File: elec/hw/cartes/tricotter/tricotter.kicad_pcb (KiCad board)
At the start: 2 copper layers, 64 parts, among them J1 XT60PW-M, J2 3-794618-4, J3 3-794618-4, J4 3-794618-4, J5 3-794618-4, J6 3-794618-4, J7 22272041, Q1 2N7002, Q10 G120P06M, Q2 G120P06M, Q3 2N7002, Q4 G120P06M, Q5 2N7002, Q6 2N7002, Q7 G120P06M, Q8 G120P06M, Q9 2N7002

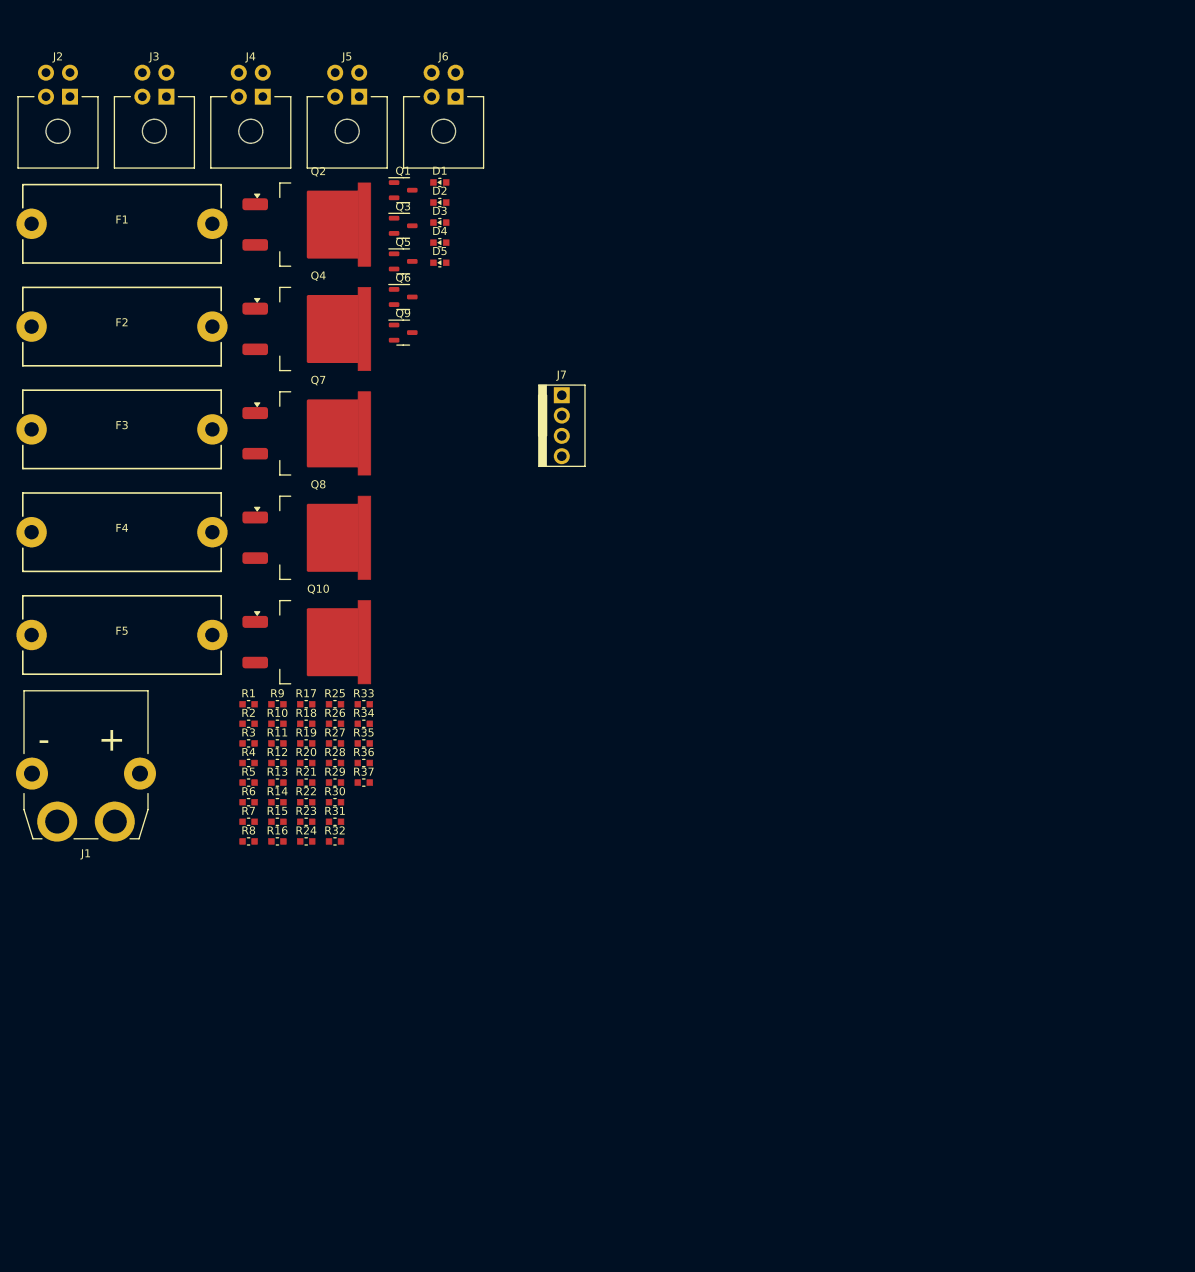
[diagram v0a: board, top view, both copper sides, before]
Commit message: tricotter board routed
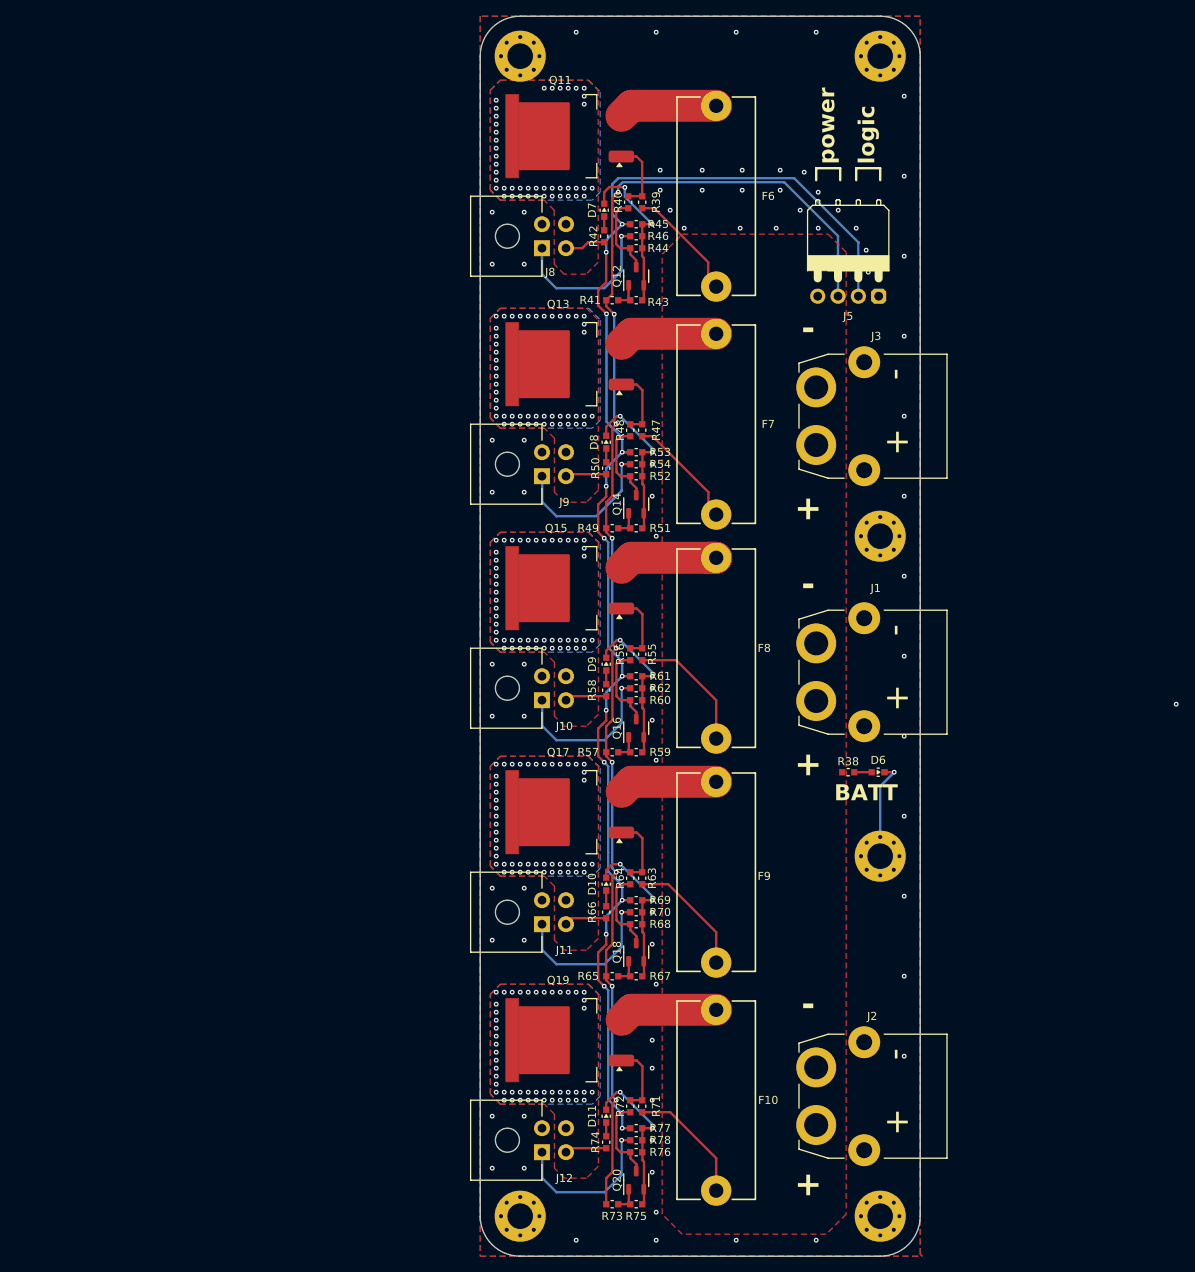
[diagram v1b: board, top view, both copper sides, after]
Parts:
- removed D1, D2, D3, D4, D5: green, 0603, cocotter_diodes:LED_0603_1608Metric
- removed F1, F2, F3, F4, F5: FH1-200CK-B, cocotter_others:FUSEHOLDER_5x20mm
- removed J4, J6: 3-794618-4, cocotter_connectors:3-794618-4
- removed J7: 22272041, cocotter_connectors:22272041
- removed Q1, Q3, Q5, Q6, Q9: 2N7002, cocotter_transistors:SOT-23-3
- removed Q10, Q2, Q4, Q7, Q8: G120P06M, cocotter_transistors:TO-263-2-GOFORD
- removed R1, R11, R12, R16, R17, R18, R19, R2, R20, R21, R25, R26, R3, R31, R32, R33, R34, R4, R5, R6: 100k, cocotter_resistor:r0603_reflow
- removed R10, R13, R14, R22, R23, R24, R28, R29, R35, R36, R7, R8: 0R, cocotter_resistor:r0603_reflow
- removed R15, R27, R30, R37, R9: 10k 1%, cocotter_resistor:r0603_reflow
- added D10: green, 0603, cocotter_diodes:LED_0603_1608Metric, F.Cu at (115.8, 133.5)
- added D11: green, 0603, cocotter_diodes:LED_0603_1608Metric, F.Cu at (115.8, 162.5)
- added D6: white, 0603, cocotter_diodes:LED_0603_1608Metric, F.Cu at (149.8, 119.5)
- added D7: green, 0603, cocotter_diodes:LED_0603_1608Metric, F.Cu at (115.5, 49.2)
- added D8: green, 0603, cocotter_diodes:LED_0603_1608Metric, F.Cu at (115.8, 78.2)
- added D9: green, 0603, cocotter_diodes:LED_0603_1608Metric, F.Cu at (115.8, 106.0)
- added F10: FH1-200CK-B, cocotter_others:FUSEHOLDER_5x20mm, F.Cu at (129.5, 160.5)
- added F6: FH1-200CK-B, cocotter_others:FUSEHOLDER_5x20mm, F.Cu at (129.5, 47.5)
- added F7: FH1-200CK-B, cocotter_others:FUSEHOLDER_5x20mm, F.Cu at (129.5, 76.0)
- added F8: FH1-200CK-B, cocotter_others:FUSEHOLDER_5x20mm, F.Cu at (129.5, 104.0)
- added F9: FH1-200CK-B, cocotter_others:FUSEHOLDER_5x20mm, F.Cu at (129.5, 132.0)
- added H1: MountingHole_Pad_M3, cocotter_others:MountingHole_3.2mm_M3_Pad_Via, F.Cu at (105.0, 175.0)
- added H2: MountingHole_Pad_M3, cocotter_others:MountingHole_3.2mm_M3_Pad_Via, F.Cu at (150.0, 175.0)
- added H3: MountingHole_Pad_M3, cocotter_others:MountingHole_3.2mm_M3_Pad_Via, F.Cu at (150.0, 30.0)
- added H4: MountingHole_Pad_M3, cocotter_others:MountingHole_3.2mm_M3_Pad_Via, F.Cu at (105.0, 30.0)
- added H5: MountingHole_Pad_M3, cocotter_others:MountingHole_3.2mm_M3_Pad_Via, F.Cu at (150.0, 90.0)
- added H6: MountingHole_Pad_M3, cocotter_others:MountingHole_3.2mm_M3_Pad_Via, F.Cu at (150.0, 130.0)
- added J10: 3-794618-4, cocotter_connectors:3-794618-4, F.Cu at (109.2, 109.0)
- added J11: 3-794618-4, cocotter_connectors:3-794618-4, F.Cu at (109.2, 137.0)
- added J12: 3-794618-4, cocotter_connectors:3-794618-4, F.Cu at (109.2, 165.5)
- added J8: 3-794618-4, cocotter_connectors:3-794618-4, F.Cu at (109.2, 52.5)
- added J9: 3-794618-4, cocotter_connectors:3-794618-4, F.Cu at (109.2, 81.0)
- added Q11: G120P06M, cocotter_transistors:TO-263-2-GOFORD, F.Cu at (109.8, 40.0)
- added Q12: 2N7002, cocotter_transistors:SOT-23-3, F.Cu at (119.5, 57.5)
- added Q13: G120P06M, cocotter_transistors:TO-263-2-GOFORD, F.Cu at (109.8, 68.5)
- added Q14: 2N7002, cocotter_transistors:SOT-23-3, F.Cu at (119.5, 86.0)
- added Q15: G120P06M, cocotter_transistors:TO-263-2-GOFORD, F.Cu at (109.8, 96.5)
- added Q16: 2N7002, cocotter_transistors:SOT-23-3, F.Cu at (119.5, 114.0)
- added Q17: G120P06M, cocotter_transistors:TO-263-2-GOFORD, F.Cu at (109.8, 124.5)
- added Q18: 2N7002, cocotter_transistors:SOT-23-3, F.Cu at (119.5, 142.0)
- added Q19: G120P06M, cocotter_transistors:TO-263-2-GOFORD, F.Cu at (109.8, 153.0)
- added Q20: 2N7002, cocotter_transistors:SOT-23-3, F.Cu at (119.5, 170.5)
- added R38: 10k 1%, cocotter_resistor:r0603_reflow, F.Cu at (146.0, 119.5)
- added R39: 100k, cocotter_resistor:r0603_reflow, F.Cu at (120.2, 48.2)
- added R40: 100k, cocotter_resistor:r0603_reflow, F.Cu at (118.5, 48.2)
- added R41: 100k, cocotter_resistor:r0603_reflow, F.Cu at (116.5, 60.5)
- added R42: 10k 1%, cocotter_resistor:r0603_reflow, F.Cu at (115.5, 52.5)
- added R43: 100k, cocotter_resistor:r0603_reflow, F.Cu at (119.5, 60.5)
- added R44: 0R, cocotter_resistor:r0603_reflow, F.Cu at (119.5, 54.0)
- added R45: 0R, cocotter_resistor:r0603_reflow, F.Cu at (119.5, 51.0)
- added R46: 0R, cocotter_resistor:r0603_reflow, F.Cu at (119.5, 52.5)
- added R47: 100k, cocotter_resistor:r0603_reflow, F.Cu at (120.2, 76.8)
- added R48: 100k, cocotter_resistor:r0603_reflow, F.Cu at (118.8, 76.8)
- added R49: 100k, cocotter_resistor:r0603_reflow, F.Cu at (116.5, 89.0)
- added R50: 10k 1%, cocotter_resistor:r0603_reflow, F.Cu at (115.8, 81.5)
- added R51: 100k, cocotter_resistor:r0603_reflow, F.Cu at (119.5, 89.0)
- added R52: 0R, cocotter_resistor:r0603_reflow, F.Cu at (119.5, 82.5)
- added R53: 0R, cocotter_resistor:r0603_reflow, F.Cu at (119.5, 79.5)
- added R54: 0R, cocotter_resistor:r0603_reflow, F.Cu at (119.5, 81.0)
- added R55: 100k, cocotter_resistor:r0603_reflow, F.Cu at (120.2, 104.8)
- added R56: 100k, cocotter_resistor:r0603_reflow, F.Cu at (118.8, 104.8)
- added R57: 100k, cocotter_resistor:r0603_reflow, F.Cu at (116.5, 117.0)
- added R58: 10k 1%, cocotter_resistor:r0603_reflow, F.Cu at (115.8, 109.2)
- added R59: 100k, cocotter_resistor:r0603_reflow, F.Cu at (119.5, 117.0)
- added R60: 0R, cocotter_resistor:r0603_reflow, F.Cu at (119.5, 110.5)
- added R61: 0R, cocotter_resistor:r0603_reflow, F.Cu at (119.5, 107.5)
- added R62: 0R, cocotter_resistor:r0603_reflow, F.Cu at (119.5, 109.0)
- added R63: 100k, cocotter_resistor:r0603_reflow, F.Cu at (120.2, 132.8)
- added R64: 100k, cocotter_resistor:r0603_reflow, F.Cu at (118.8, 132.8)
- added R65: 100k, cocotter_resistor:r0603_reflow, F.Cu at (116.5, 145.0)
- added R66: 10k 1%, cocotter_resistor:r0603_reflow, F.Cu at (115.8, 137.0)
- added R67: 100k, cocotter_resistor:r0603_reflow, F.Cu at (119.5, 145.0)
- added R68: 0R, cocotter_resistor:r0603_reflow, F.Cu at (119.5, 138.5)
- added R69: 0R, cocotter_resistor:r0603_reflow, F.Cu at (119.5, 135.5)
- added R70: 0R, cocotter_resistor:r0603_reflow, F.Cu at (119.5, 137.0)
- added R71: 100k, cocotter_resistor:r0603_reflow, F.Cu at (120.2, 161.2)
- added R72: 100k, cocotter_resistor:r0603_reflow, F.Cu at (118.8, 161.2)
- added R73: 100k, cocotter_resistor:r0603_reflow, F.Cu at (116.5, 173.5)
- added R74: 10k 1%, cocotter_resistor:r0603_reflow, F.Cu at (115.8, 165.8)
- added R75: 100k, cocotter_resistor:r0603_reflow, F.Cu at (119.5, 173.5)
- added R76: 0R, cocotter_resistor:r0603_reflow, F.Cu at (119.5, 167.0)
- added R77: 0R, cocotter_resistor:r0603_reflow, F.Cu at (119.5, 164.0)
- added R78: 0R, cocotter_resistor:r0603_reflow, F.Cu at (119.5, 165.5)
- J2, J3: value 3-794618-4 -> XT60PW-M; footprint cocotter_connectors:3-794618-4 -> cocotter_connectors:XT60PW-M
- J5: value 3-794618-4 -> 22053041; footprint cocotter_connectors:3-794618-4 -> cocotter_connectors:22053041
- moved J2 158.0 mm to (142.0, 160.0), turned to -90 degrees
- moved J1 93.2 mm to (142.0, 107.0), turned to -90 degrees
- moved J3 92.5 mm to (142.0, 75.0), turned to -90 degrees
- moved J5 68.0 mm to (146.0, 60.0), turned to 180 degrees
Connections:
- J2 pad 4: Net-(Q2-D) -> (no net)
- J3 pad 4: Net-(Q4-D) -> (no net)
- J5 pad 2: GND -> /SW_logical
- J5 pad 3: Net-(Q8-D) -> /SW_POWER
- J5 pad 4: Net-(Q8-D) -> +BATT
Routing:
- net /SW_logical: track 0.00 -> 174.6 mm, vias 0 -> 13
- net /SW_POWER: track 0.00 -> 170.0 mm, vias 0 -> 9
- net GND: track 0.00 -> 113.0 mm, vias 0 -> 82
- net +BATT: track 0.00 -> 75.3 mm
- net Net-(Q12-S): track 0.00 -> 21.3 mm, vias 0 -> 2
- net Net-(Q14-S): track 0.00 -> 20.7 mm, vias 0 -> 2
- net Net-(Q16-S): track 0.00 -> 20.5 mm, vias 0 -> 2
- net Net-(Q20-S): track 0.00 -> 20.5 mm, vias 0 -> 2
- net Net-(Q18-S): track 0.00 -> 20.1 mm, vias 0 -> 2
- net Net-(Q15-S): track 0.00 -> 13.3 mm
- net Net-(Q19-S): track 0.00 -> 12.4 mm
- net Net-(Q17-S): track 0.00 -> 12.4 mm
- net Net-(Q13-S): track 0.00 -> 12.4 mm
- net Net-(Q11-S): track 0.00 -> 12.4 mm
- net Net-(Q20-D): track 0.00 -> 10.6 mm
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- added copper zone on F.Cu, net +BATT
- added copper zone on B.Cu, net GND
- added copper zone on F.Cu, net GND
- added copper zone on B.Cu, net Net-(Q11-D)
- added copper zone on F.Cu, net Net-(Q11-D)
- added copper zone on B.Cu, net Net-(Q13-D)
- added copper zone on F.Cu, net Net-(Q13-D)
- added copper zone on B.Cu, net Net-(Q15-D)
- added copper zone on F.Cu, net Net-(Q15-D)
- added copper zone on B.Cu, net Net-(Q17-D)
- added copper zone on F.Cu, net Net-(Q17-D)
- added copper zone on B.Cu, net Net-(Q19-D)
- added copper zone on F.Cu, net Net-(Q19-D)
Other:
- board outline added: 55 x 155 mm
- board text added: "+"
- board text added: "-"
- board text added: "BATT"
- board text added: "logic"
- board text added: "power"

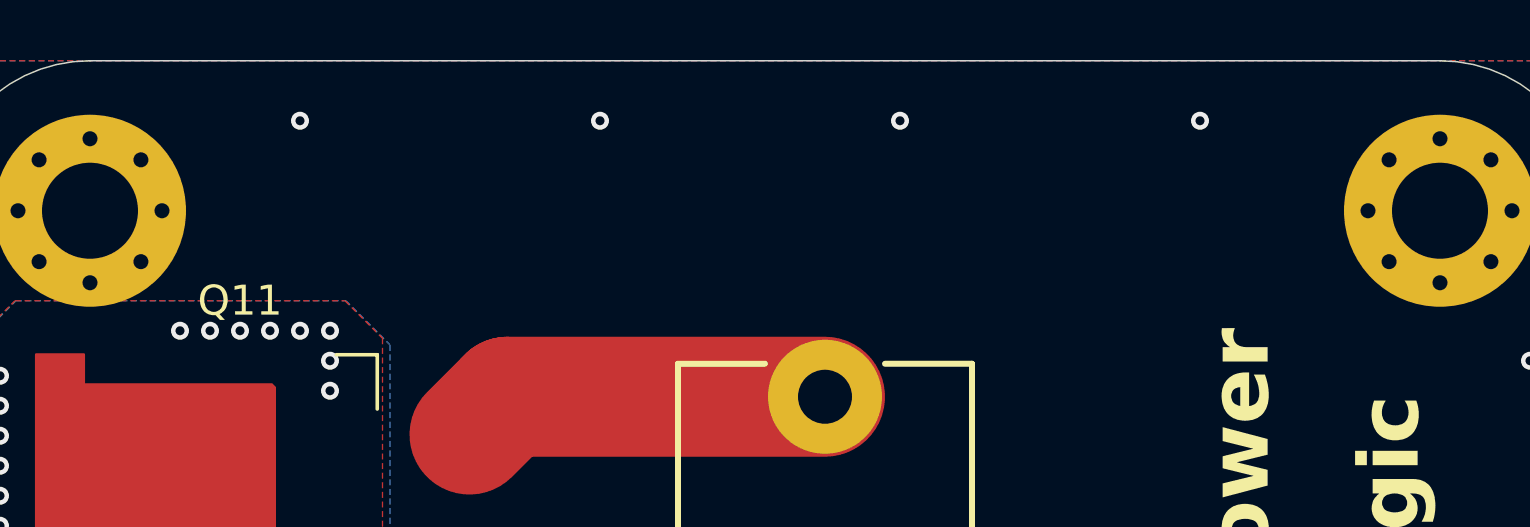
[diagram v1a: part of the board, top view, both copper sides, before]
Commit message: board name added
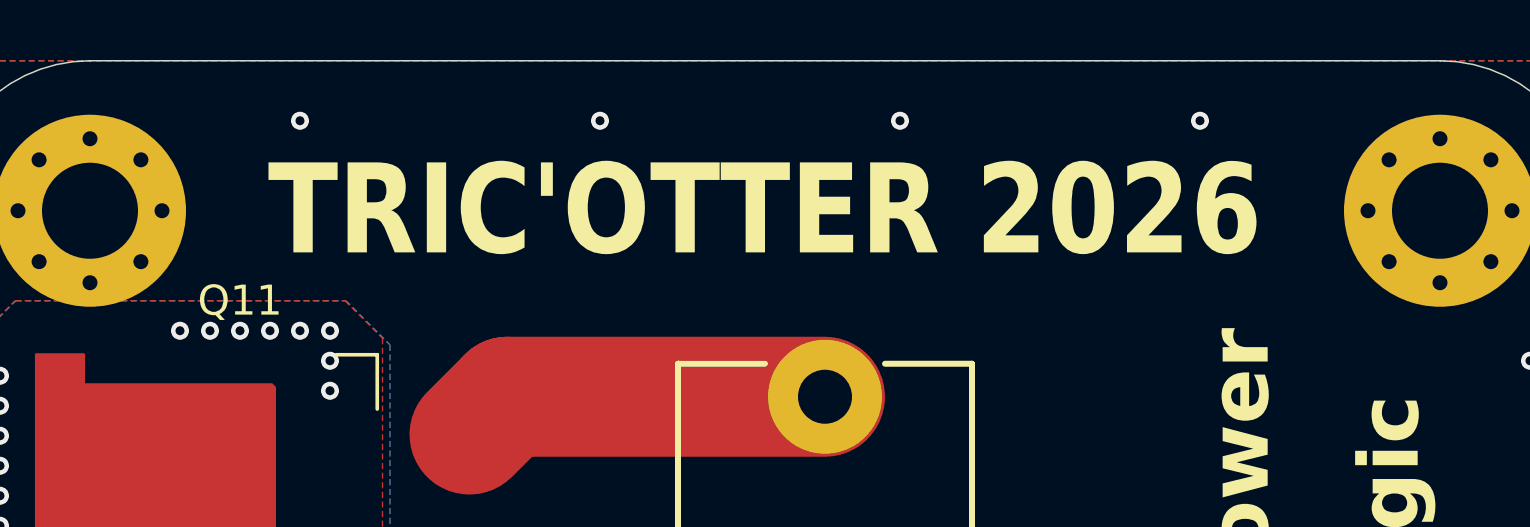
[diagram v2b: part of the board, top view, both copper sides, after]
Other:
- board text added: "TRIC'OTTER 2026"
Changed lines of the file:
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@@
+		)
+	)
+	(gr_text "TRIC'OTTER 2026"
+		(at 127.5 30 0)
+		(layer "F.SilkS" knockout)
+		(effects
+			(font
+				(size 3 2.5)
+				(thickness 0.5)
+				(bold yes)
+			)
 		)
 	)
